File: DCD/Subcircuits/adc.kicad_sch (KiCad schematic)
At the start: 5 parts, among them U1 AD4630-24BBCZ

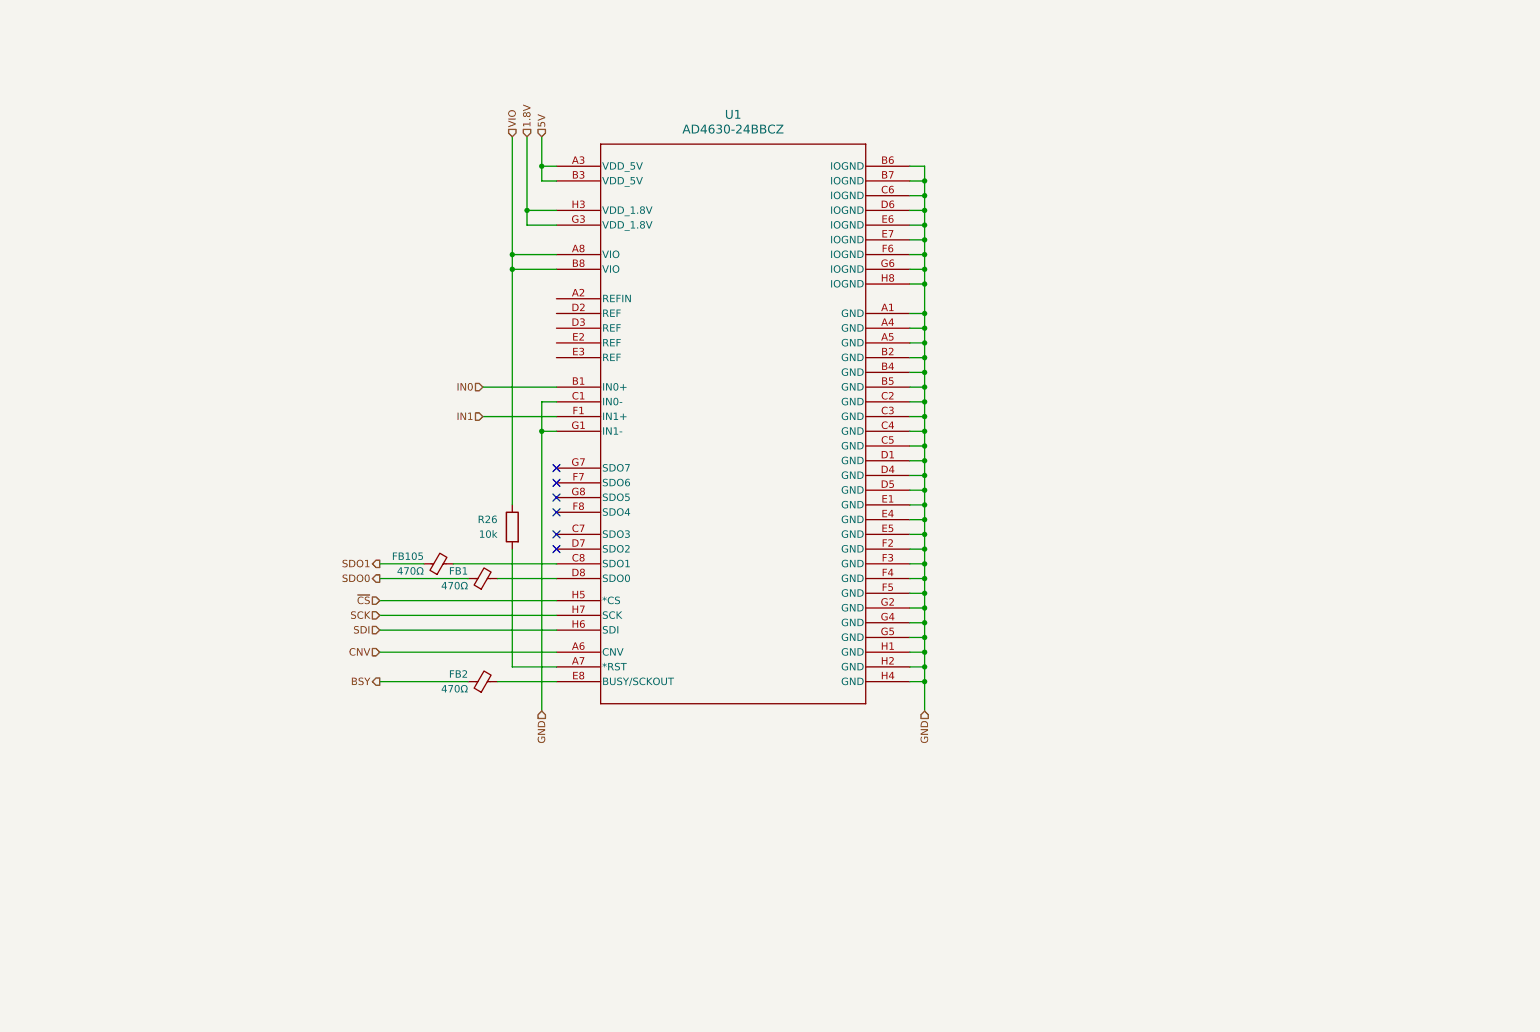
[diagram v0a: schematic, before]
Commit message: Added the Vref supply, finished all of the top level connections
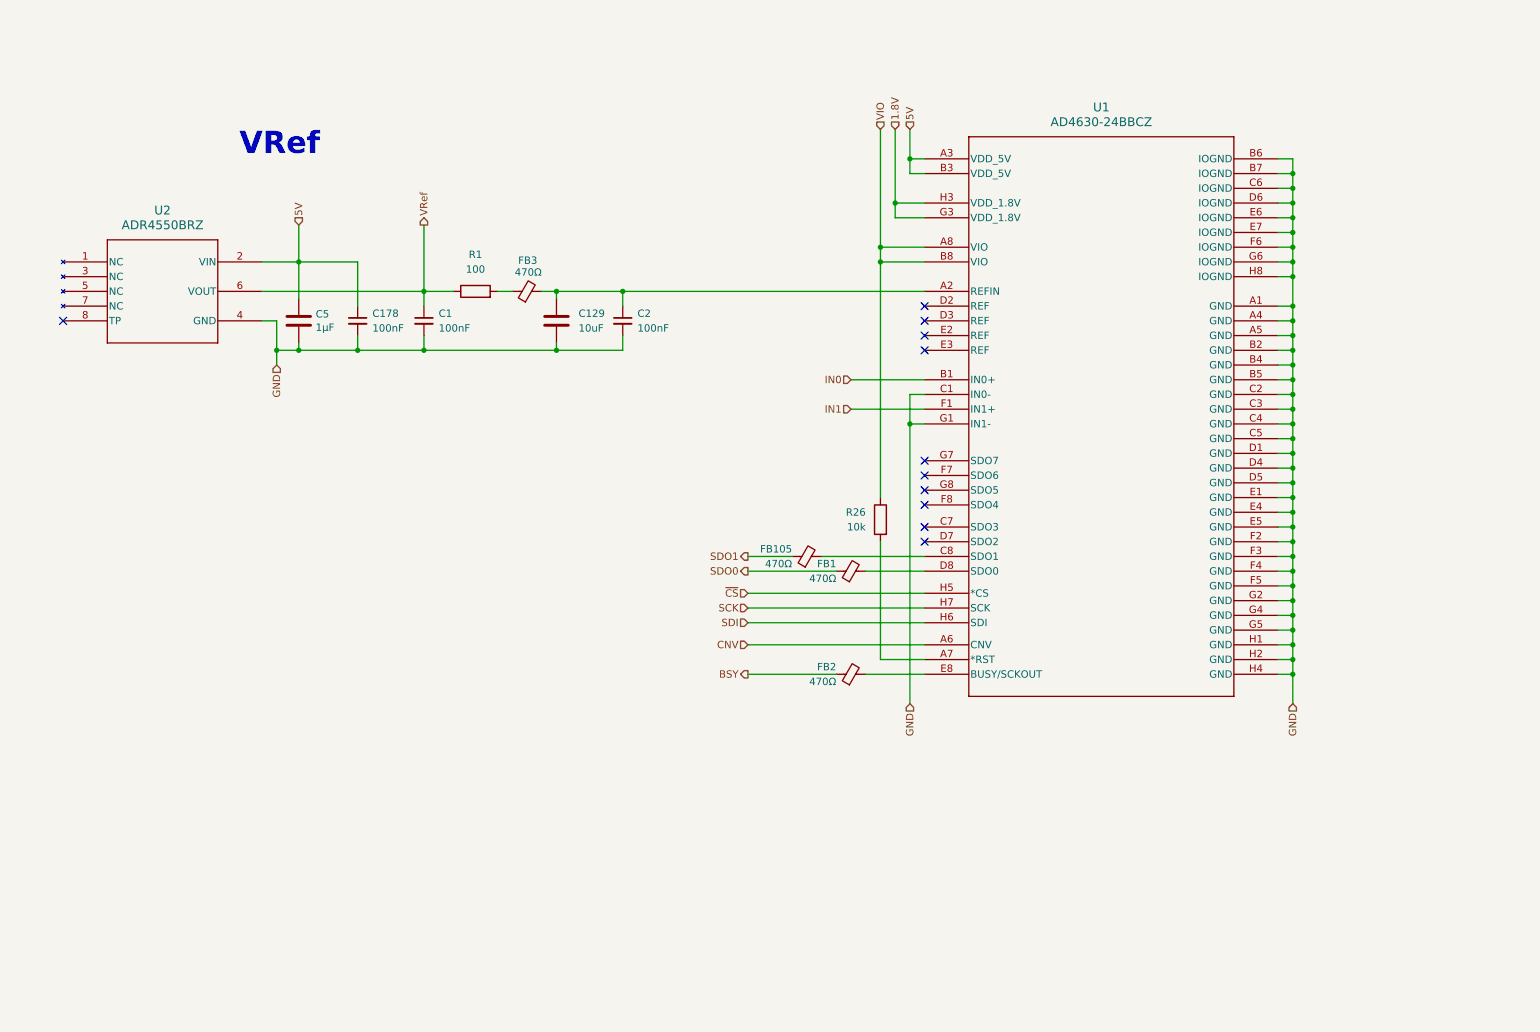
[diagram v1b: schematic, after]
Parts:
- added C1, C178, C2: 100nF, Capacitor_SMD:C_0603_1608Metric, symbol Device:C_Small
- added C129: 10uF, Capacitor_SMD:C_1210_3225Metric, symbol Device:C
- added C5: 1µF, Capacitor_SMD:C_0603_1608Metric, symbol Device:C
- added FB3: 470Ω, Inductor_SMD:L_0603_1608Metric, symbol Device:FerriteBead_Small
- added R1: 100, Resistor_SMD:R_0603_1608Metric, symbol Device:R
- added U2: ADR4550BRZ, R_8_ADI, symbol custom_components:ADR4550BRZ
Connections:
- net 5V: now also C178.1, C5.1, U2.2 (VIN)
- net GND: now also C1.2, C129.2, C178.2, C2.2, C5.2, U2.4 (GND)
- net at U1.A2 (REFIN): now also C129.1, C2.1, FB3.2
- new net: FB3.1, R1.2
- new net VRef: C1.1, R1.1, U2.6 (VOUT)
- no-connect marks 6 -> 11
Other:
- note added: "VRef"
- moved on the sheet: FB1, FB105, FB2, R26, U1

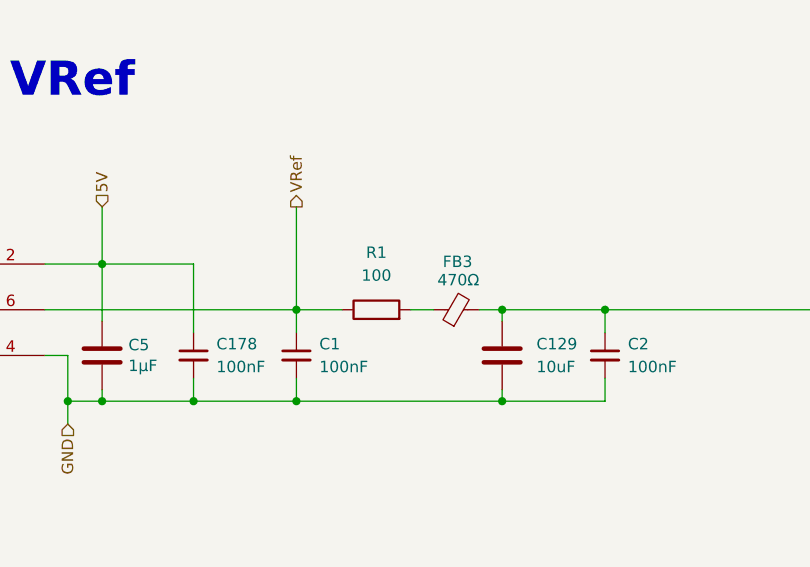
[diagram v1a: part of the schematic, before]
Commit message: Did the signal switching, finished ADC, misc changes to top
Decided to go with solder jumpers instead of power switches bc power
switches have no specs of linearity and they would add unnecessary
complexity, development time, and routing problems.

The calibration test has to be done only once and the chamber doesn't
even have to be sealed for it, so it shouldn't add too much hassle.
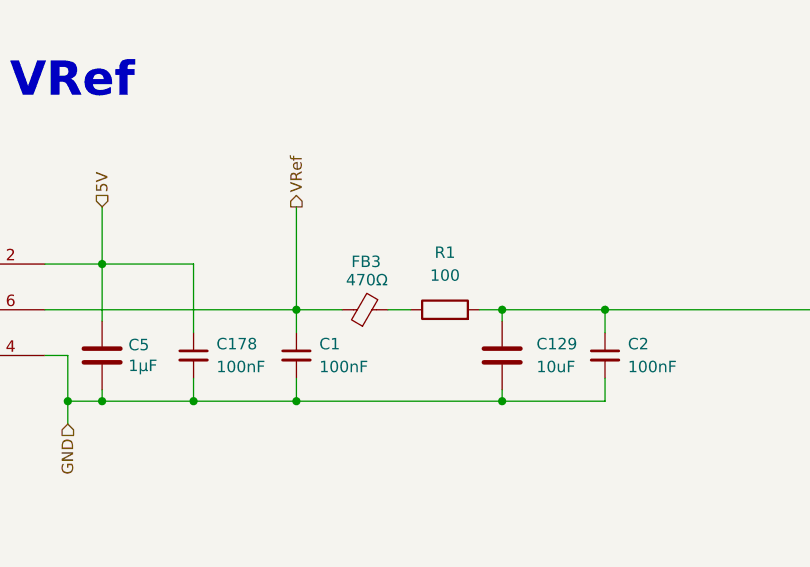
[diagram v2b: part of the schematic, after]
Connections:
- net VRef: now also FB3.1; no longer R1.1
- net at C129.1, C2.1, U1.A2 (REFIN): now also R1.2; no longer FB3.2
- new net: FB3.2, R1.1
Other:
- moved on the sheet: FB3, R1
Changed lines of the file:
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@@
-	(wire
-		(pts
-			(xy 101.6 66.04) (xy 104.14 66.04)
-		)
-		(stroke
-			(width 0)
-			(type default)
-		)
-	)
 	(wire
 		(pts
@@
 		(pts
 			(xy 238.76 58.42) (xy 238.76 60.96)
+		)
+		(stroke
+			(width 0)
+			(type default)
+		)
+	)
+	(wire
+		(pts
+			(xy 99.06 66.04) (xy 101.6 66.04)
 		)
 		(stroke
@@
 	(symbol
 		(lib_id "Device:FerriteBead_Small")
-		(at 106.68 66.04 90)
+		(at 96.52 66.04 90)
 		(unit 1)
 		(exclude_from_sim no)
@@
 		(dnp no)
 		(property "Reference" "FB3"
-			(at 108.458 60.706 90)
+			(at 98.298 60.706 90)
 			(effects
 				(font
@@
 		)
 		(property "Value" "470Ω"
-			(at 109.22 62.738 90)
+			(at 99.06 62.738 90)
 			(effects
 				(font
@@
 		)
 		(property "Footprint" "Inductor_SMD:L_0603_1608Metric"
-			(at 106.68 67.818 90)
+			(at 96.52 67.818 90)
 			(effects
 				(font
@@
 		)
 		(property "Datasheet" "~"
-			(at 106.68 66.04 0)
+			(at 96.52 66.04 0)
 			(effects
 				(font
@@
 		)
 		(property "Description" "Ferrite bead, small symbol"
-			(at 106.68 66.04 0)
+			(at 96.52 66.04 0)
 			(effects
 				(font
@@
 		)
 		(property "Part number" "BLM18GG471SN1D"
-			(at 106.68 66.04 90)
+			(at 96.52 66.04 90)
 			(effects
 				(font
@@
 		)
 		(property "Order number" "81-BLM18GG471SN1D"
-			(at 106.68 66.04 90)
+			(at 96.52 66.04 90)
 			(effects
 				(font
@@
 		)
 		(property "Supplier" "Mouser"
-			(at 106.68 66.04 90)
+			(at 96.52 66.04 90)
 			(effects
 				(font
@@
 		)
 		(property "Link" "https://eu.mouser.com/ProductDetail/Murata-Electronics/BLM18GG471SN1D?qs=uSeJpk%2F8In1VmERn9ukNjA%3D%3D"
-			(at 106.68 66.04 90)
+			(at 96.52 66.04 90)
 			(effects
 				(font
@@
 		)
 		(instances
-			(project ""
+			(project "DCD"
 				(path "/b8e3d55b-fa56-4199-88ad-60cfd98f56f9/a2b5f9c0-8e7d-4b76-a173-d00aba9c5441"
 					(reference "U2")
@@
 	(symbol
 		(lib_id "Device:R")
-		(at 97.79 66.04 90)
+		(at 105.41 66.04 90)
 		(unit 1)
 		(exclude_from_sim no)
@@
 		(fields_autoplaced yes)
 		(property "Reference" "R1"
-			(at 97.79 59.69 90)
+			(at 105.41 59.69 90)
 			(effects
 				(font
@@
 		)
 		(property "Value" "100"
-			(at 97.79 62.23 90)
+			(at 105.41 62.23 90)
 			(effects
 				(font
@@
 		)
 		(property "Footprint" "Resistor_SMD:R_0603_1608Metric"
-			(at 97.79 67.818 90)
+			(at 105.41 67.818 90)
 			(effects
 				(font
@@
 		)
 		(property "Datasheet" "~"
-			(at 97.79 66.04 0)
+			(at 105.41 66.04 0)
 			(effects
 				(font
@@
 		)
 		(property "Description" "Resistor"
-			(at 97.79 66.04 0)
+			(at 105.41 66.04 0)
 			(effects
 				(font
@@
 		)
 		(property "Link " "https://eu.mouser.com/ProductDetail/Panasonic/ERA-3VEB1000V?qs=sGAEpiMZZMtlubZbdhIBIFX24rZb7BVEWmP2JDQu%252BM0%3D"
-			(at 97.79 66.04 90)
+			(at 105.41 66.04 90)
 			(effects
 				(font
@@
 		)
 		(instances
-			(project ""
+			(project "DCD"
 				(path "/b8e3d55b-fa56-4199-88ad-60cfd98f56f9/a2b5f9c0-8e7d-4b76-a173-d00aba9c5441"
 					(reference "R1")

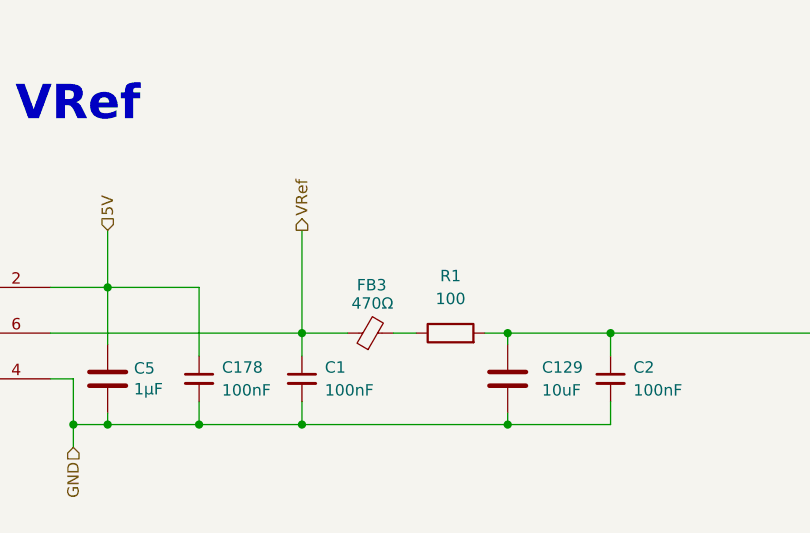
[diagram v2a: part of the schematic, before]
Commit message: Finished switches, added calculations of the current consumption
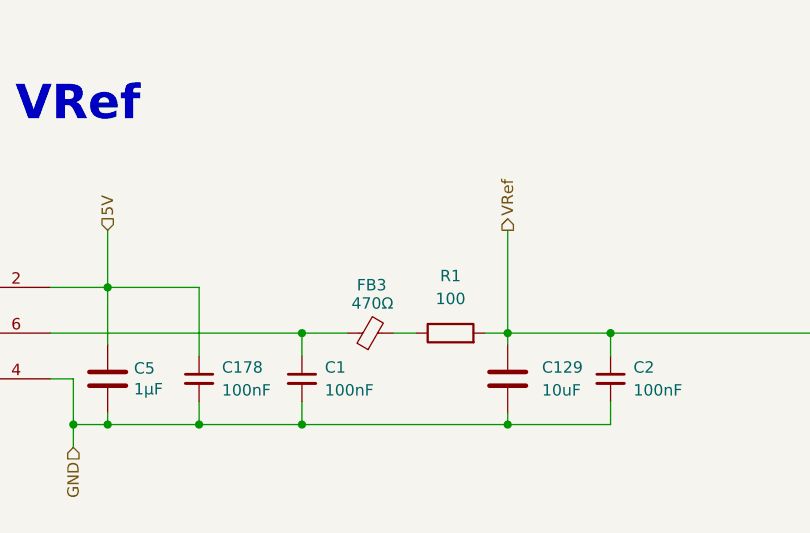
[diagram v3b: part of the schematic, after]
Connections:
- net VRef: now also C129.1, C2.1, R1.2, U1.A2 (REFIN); no longer C1.1, FB3.1, U2.6 (VOUT)
- new net: C1.1, FB3.1, U2.6 (VOUT)
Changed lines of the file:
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@@
-	(wire
-		(pts
-			(xy 88.9 54.61) (xy 88.9 66.04)
-		)
-		(stroke
-			(width 0)
-			(type default)
-		)
-	)
 	(wire
 		(pts
@@
 		(pts
 			(xy 157.48 111.76) (xy 175.26 111.76)
+		)
+		(stroke
+			(width 0)
+			(type default)
+		)
+	)
+	(wire
+		(pts
+			(xy 111.76 54.61) (xy 111.76 66.04)
 		)
 		(stroke
@@
 	(hierarchical_label "VRef"
 		(shape output)
-		(at 88.9 54.61 90)
-		(effects
-			(font
+		(at 111.76 54.61 90)
+		(effects
+			(font

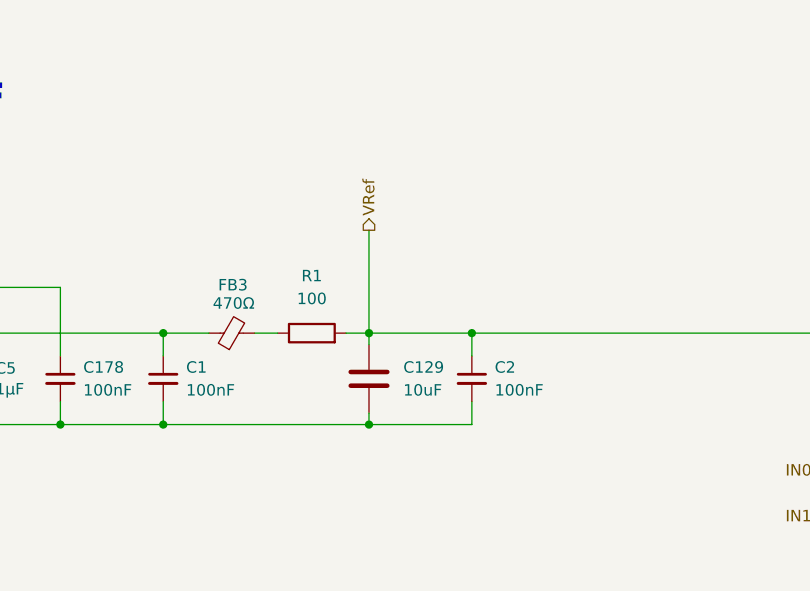
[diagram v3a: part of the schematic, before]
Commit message: Added PSUS, progress on the PSU circuit design, slight tweaks to the rest
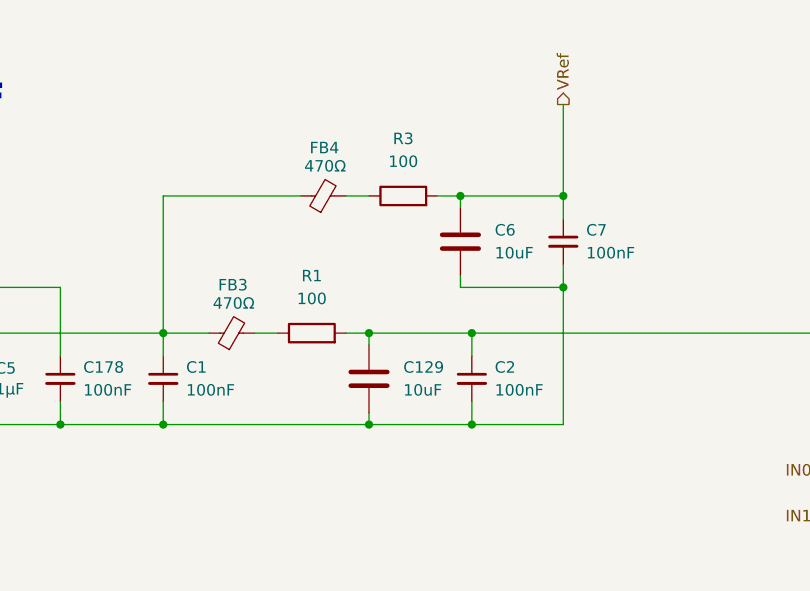
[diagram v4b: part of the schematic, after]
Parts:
- added C6: 10uF, Capacitor_SMD:C_1210_3225Metric, symbol Device:C
- added C7: 100nF, Capacitor_SMD:C_0603_1608Metric, symbol Device:C_Small
- added FB4: 470Ω, Inductor_SMD:L_0603_1608Metric, symbol Device:FerriteBead_Small
- added R3: 100, Resistor_SMD:R_0603_1608Metric, symbol Device:R
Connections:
- net GND: now also C6.2, C7.2
- net VRef: now also C6.1, C7.1, R3.2; no longer C129.1, C2.1, R1.2, U1.A2 (REFIN)
- net at C1.1, FB3.1, U2.6 (VOUT): now also FB4.1
- new net: C129.1, C2.1, R1.2, U1.A2 (REFIN)
- new net: FB4.2, R3.1
